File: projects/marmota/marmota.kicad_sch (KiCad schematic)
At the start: 58 parts, among them J1 USB_C, J2 Conn_01x20_Pin, J3 Conn_01x20_Pin, SW1 Button top, SW2 Button side, U1 RP2040, U2 FLASH, U3 MCP73871, U4 RT6150B, U5 ESP32, Y1 12MHz

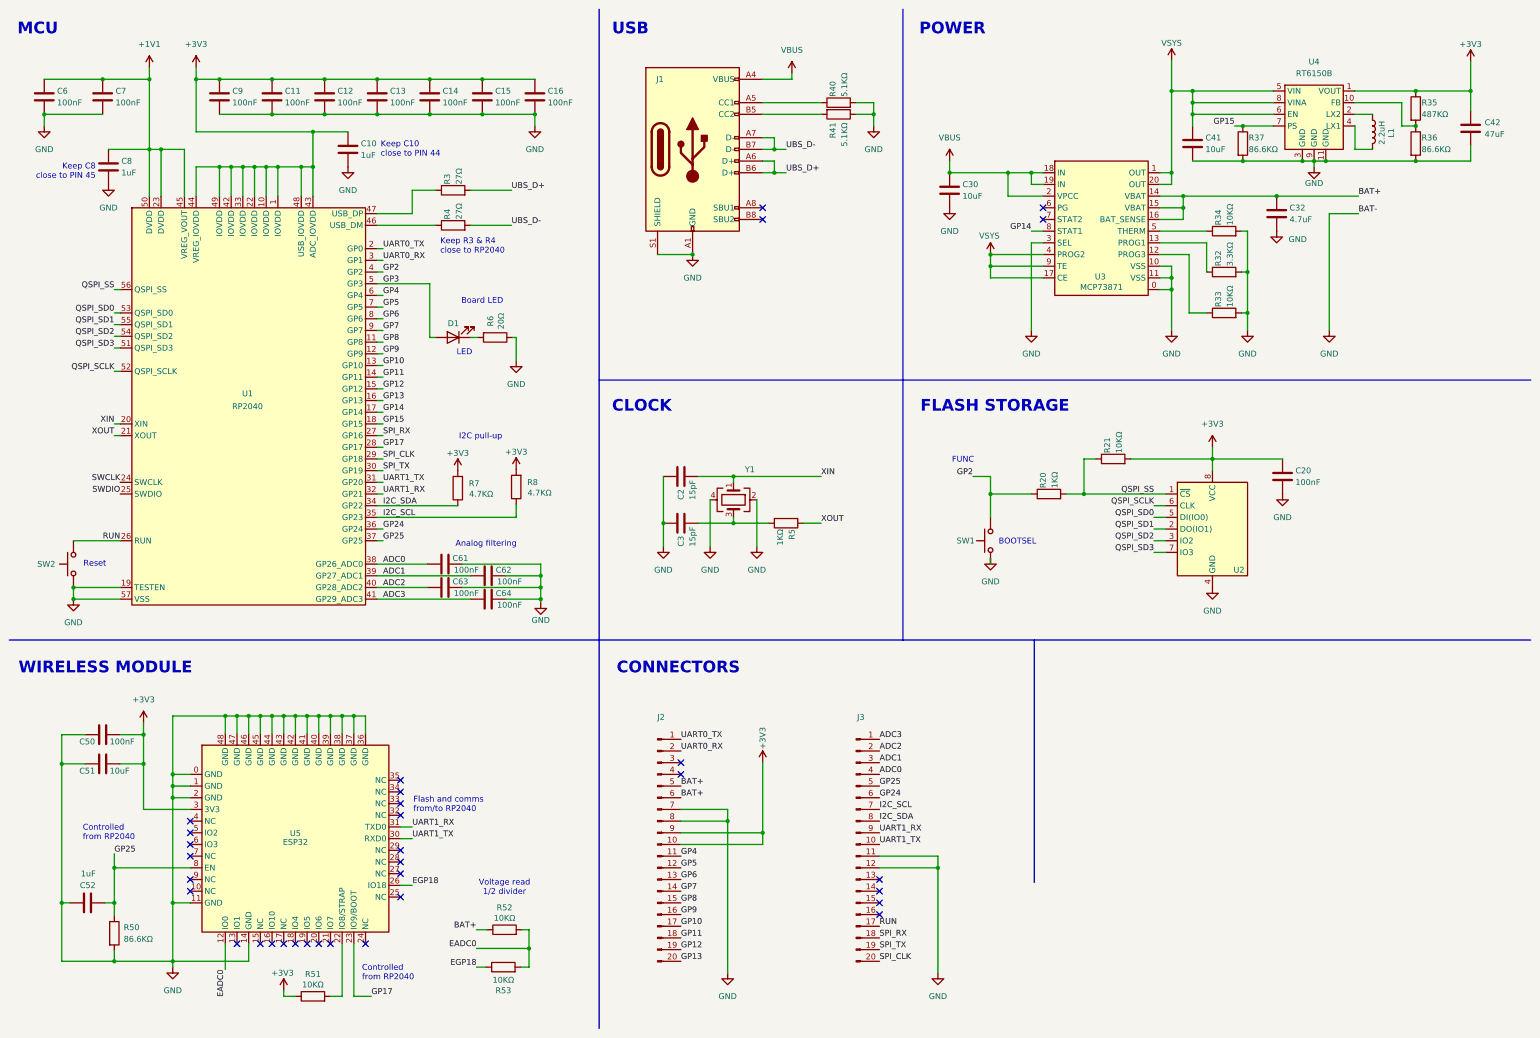
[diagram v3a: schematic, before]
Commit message: Initial schematic for nRF52840+nPM1300
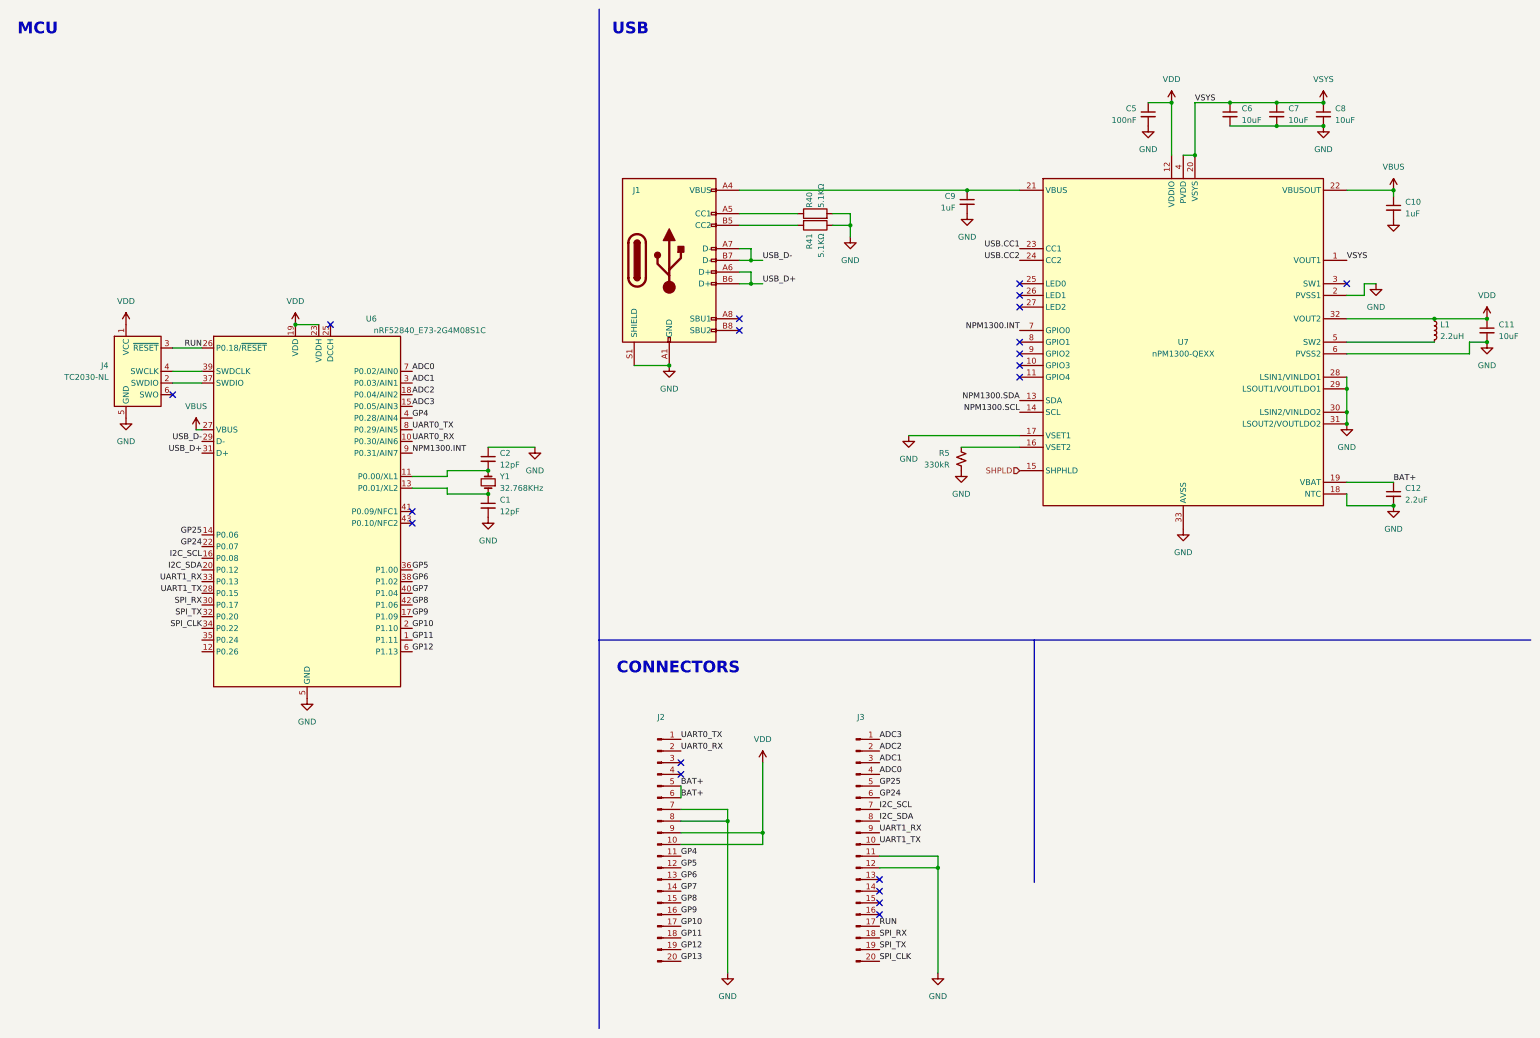
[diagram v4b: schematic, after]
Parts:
- removed C10, C52, C8: 1uF, ILO_fp:0402_compact, symbol Device:C
- removed C11, C12, C13, C14, C15, C16, C20, C50, C6, C61, C62, C63, C64, C7, C9: 100nF, ILO_fp:0402_compact, symbol Device:C
- removed C2, C3: 15pF, ILO_fp:0402_compact, symbol Device:C
- removed C30, C41, C51: 10uF, ILO_fp:0402_compact, symbol Device:C
- removed C32: 4.7uF, ILO_fp:0402_compact, symbol Device:C
- removed C42: 47uF, ILO_fp:0603_compact, symbol Device:C
- removed D1: Diode, ILO_fp:0603_d, symbol Device:LED
- removed L1: 2.2uH, ILO_fp:0603_compact, symbol Device:L
- removed R20, R5: 1KΩ, ILO_fp:0402_compact, symbol Device:R
- removed R21, R33, R34, R51, R52, R53: 10KΩ, ILO_fp:0402_compact, symbol Device:R
- removed R3, R4: 27Ω, ILO_fp:0402_compact, symbol Device:R
- removed R32: 3.3KΩ, ILO_fp:0402_compact, symbol Device:R
- removed R35: 487KΩ, ILO_fp:0402_compact, symbol Device:R
- removed R36, R37, R50: 86.6KΩ, ILO_fp:0402_compact, symbol Device:R
- removed R6: 20Ω, ILO_fp:0603, symbol Device:R
- removed R7, R8: 4.7KΩ, ILO_fp:0402_compact, symbol Device:R
- removed SW1: Button top, ILO_fp:Alpsalpine_SKRP_compact, symbol Switch:SW_Push
- removed SW2: Button side, ILO_fp:Alpsalpine_SKSC, symbol Switch:SW_Push
- removed U1: RP2040, Package_DFN_QFN:QFN-56-1EP_7x7mm_P0.4mm_EP3.2x3.2mm, symbol ILO_sym:Raspberry_RP2040
- removed U2: FLASH, ILO_fp:Winbond_W25Q, symbol Memory_Flash:W25Q128JVS
- removed U3: MCP73871, ILO_fp:QFN20_internal_routing, symbol ILO_sym:Microchip_MCP73871
- removed U4: RT6150B, ILO_fp:WDFN-10L-2.5x2.5, symbol ILO_sym:Richtek_RT6150
- removed U5: ESP32, ILO_fp:Espressif_ESP32_mini, symbol ILO_sym:Espressif_ESP8684_mini
- removed Y1: 12MHz, Crystal:Crystal_SMD_2520-4Pin_2.5x2.0mm, symbol Device:Crystal_GND24
- added C1, C2: 12pF, symbol Device:C_Small
- added C10, C9: 1uF, Capacitor_SMD:C_0603_1608Metric, symbol Device:C_Small
- added C11, C6, C7, C8: 10uF, Capacitor_SMD:C_0603_1608Metric, symbol Device:C_Small
- added C12: 2.2uF, Capacitor_SMD:C_0603_1608Metric, symbol Device:C_Small
- added C5: 100nF, Capacitor_SMD:C_0402_1005Metric, symbol Device:C_Small
- added J4: TC2030-NL, Connector:Tag-Connect_TC2030-IDC-NL_2x03_P1.27mm_Vertical, symbol Connector:Conn_ARM_SWD_TagConnect_TC2030-NL
- added L1: 2.2uH, Inductor_SMD:L_0603_1608Metric, symbol Device:L_Small
- added R5: 330kR, Resistor_SMD:R_0402_1005Metric, symbol Device:R_Small_US
- added U6: nRF52840_E73-2G4M08S1C, PCM_marbastlib-various:nRF52840_E73-2G4M08S1C, symbol PCM_marbastlib-various:nRF52840_E73-2G4M08S1C
- added U7: nPM1300-QEXX, Package_DFN_QFN:QFN-32-1EP_5x5mm_P0.5mm_EP3.6x3.6mm_ThermalVias, symbol nordic-lib-kicad-npm:nPM1300-QEXX
- added Y1: 32.768KHz, symbol Device:Crystal_Small
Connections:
- net ADC0: now also U6.7 (P0.02/AIN0)
- net ADC1: now also U6.3 (P0.03/AIN1)
- net ADC2: now also U6.18 (P0.04/AIN2)
- net ADC3: now also U6.15 (P0.05/AIN3)
- net BAT+: now also C12.1, U7.19 (VBAT)
- net GND: now also C1.2, C10.2, C11.2, C12.2, C2.1, C5.2, C6.2, C7.2, C8.2, C9.2, J4.5 (GND), R5.2, U6.21 (GND), U6.24 (GND), U6.5 (GND), U7.17 (VSET1), U7.18 (NTC), U7.2 (PVSS1), U7.28 (LSIN1/VINLDO1), U7.29 (LSOUT1/VOUTLDO1), U7.30 (LSIN2/VINLDO2), U7.31 (LSOUT2/VOUTLDO2), U7.33 (AVSS), U7.6 (PVSS2)
- net GP10: now also U6.2 (P1.10)
- net GP11: now also U6.1 (P1.11)
- net GP12: now also U6.6 (P1.13)
- net GP24: now also U6.22 (P0.07)
- net GP25: now also U6.14 (P0.06)
- net GP4: now also U6.4 (P0.28/AIN4)
- net GP5: now also U6.36 (P1.00)
- net GP6: now also U6.38 (P1.02)
- net GP7: now also U6.40 (P1.04)
- net GP8: now also U6.42 (P1.06)
- net GP9: now also U6.17 (P1.09)
- net I2C_SCL: now also U6.16 (P0.08)
- net I2C_SDA: now also U6.20 (P0.12)
- net RUN: now also J4.3 (~{RESET}), U6.26 (P0.18/~{RESET})
- net SPI_CLK: now also U6.34 (P0.22)
- net SPI_RX: now also U6.30 (P0.17)
- net SPI_TX: now also U6.32 (P0.20)
- net UART0_RX: now also U6.10 (P0.30/AIN6)
- net UART0_TX: now also U6.8 (P0.29/AIN5)
- net UART1_RX: now also U6.33 (P0.13)
- net UART1_TX: now also U6.28 (P0.15)
- net VBUS: now also C10.1, U6.27 (VBUS), U7.22 (VBUSOUT); no longer J1.A4 (VBUS), J1.A9 (VBUS), J1.B4 (VBUS), J1.B9 (VBUS)
- net VSYS: now also C6.1, C7.1, C8.1, U7.1 (VOUT1), U7.20 (VSYS), U7.4 (PVDD)
- net +3V3 renamed VDD
- net VDD: now also C11.1, C5.1, J4.1 (VCC), L1.1, U6.19 (VDD), U6.23 (VDDH), U7.12 (VDDIO), U7.32 (VOUT2)
- net UBS_D+ renamed USB_D+
- net USB_D+: now also U6.31 (D+)
- net UBS_D- renamed USB_D-
- net USB_D-: now also U6.29 (D-)
- new net: L1.2, U7.5 (SW2)
- new net: J4.2 (SWDIO), U6.37 (SWDIO)
- new net: J4.4 (SWCLK), U6.39 (SWDCLK)
- new net: C9.1, J1.A4 (VBUS), J1.A9 (VBUS), J1.B4 (VBUS), J1.B9 (VBUS), U7.21 (VBUS)
- new net: C1.1, U6.13 (P0.01/XL2), Y1.1
- new net: C2.2, U6.11 (P0.00/XL1), Y1.2
- new net: R5.1, U7.16 (VSET2)
- new net NPM1300.INT: U6.9 (P0.31/AIN7), U7.7 (GPIO0)
- new net NPM1300.SCL: U7.14 (SCL)
- new net NPM1300.SDA: U7.13 (SDA)
- new net SHPLD: U7.15 (SHPHLD)
- new net USB.CC1: U7.23 (CC1)
- new net USB.CC2: U7.24 (CC2)
- no-connect marks 33 -> 20
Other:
- note removed: "Analog filtering"
- note removed: "BOOTSEL"
- note removed: "Board LED"
- note removed: "CLOCK"
- note removed: "Controlled from RP2040"
- note removed: "FLASH STORAGE"
- note removed: "FUNC"
- note removed: "Flash and comms from/to RP2040"
- note removed: "I2C pull-up"
- note removed: "Keep C10 close to PIN 44"
- note removed: "Keep C8 close to PIN 45"
- note removed: "Keep R3 & R4 close to RP2040"
- note removed: "LED"
- note removed: "POWER"
- note removed: "Reset"
- note removed: "Voltage read 1/2 divider"
- note removed: "WIRELESS MODULE"
- moved on the sheet: J1, R40, R41

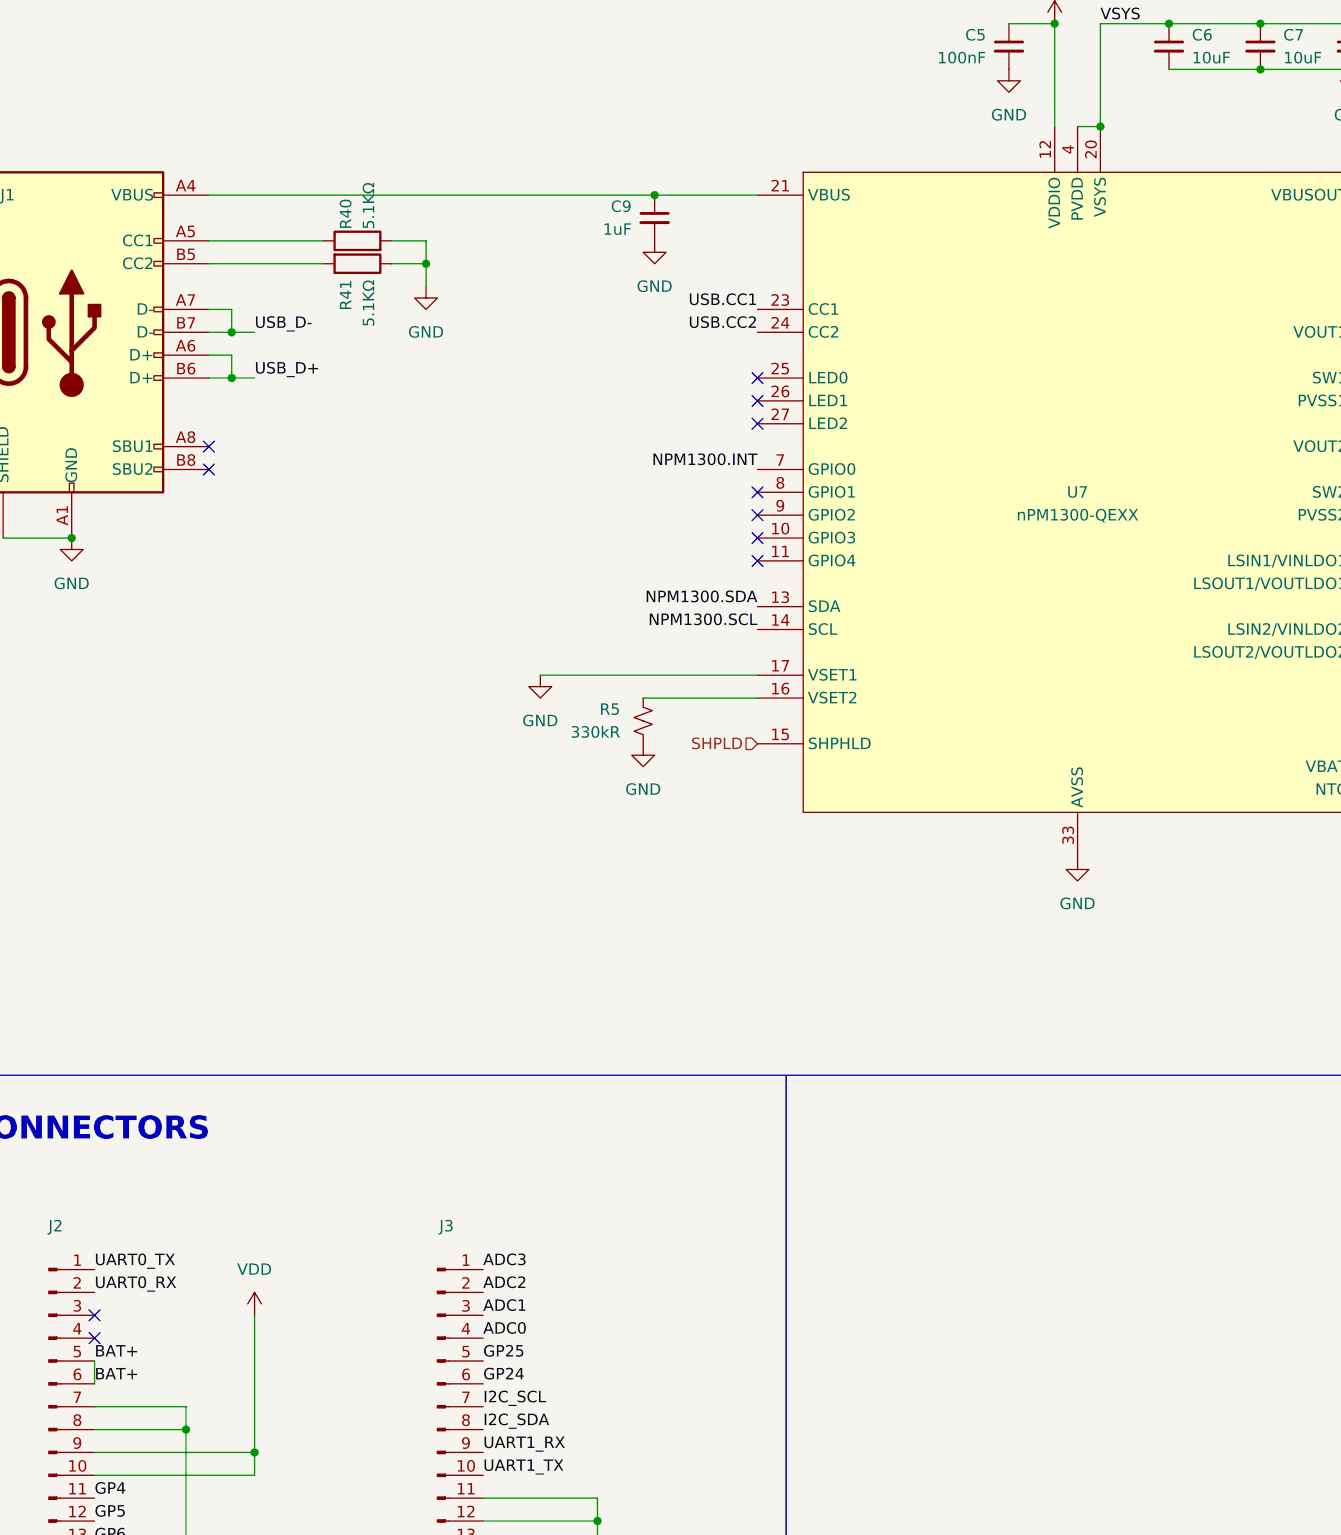
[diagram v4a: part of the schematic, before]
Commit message: Reworked Alpakka w/ interrupt lines, etc
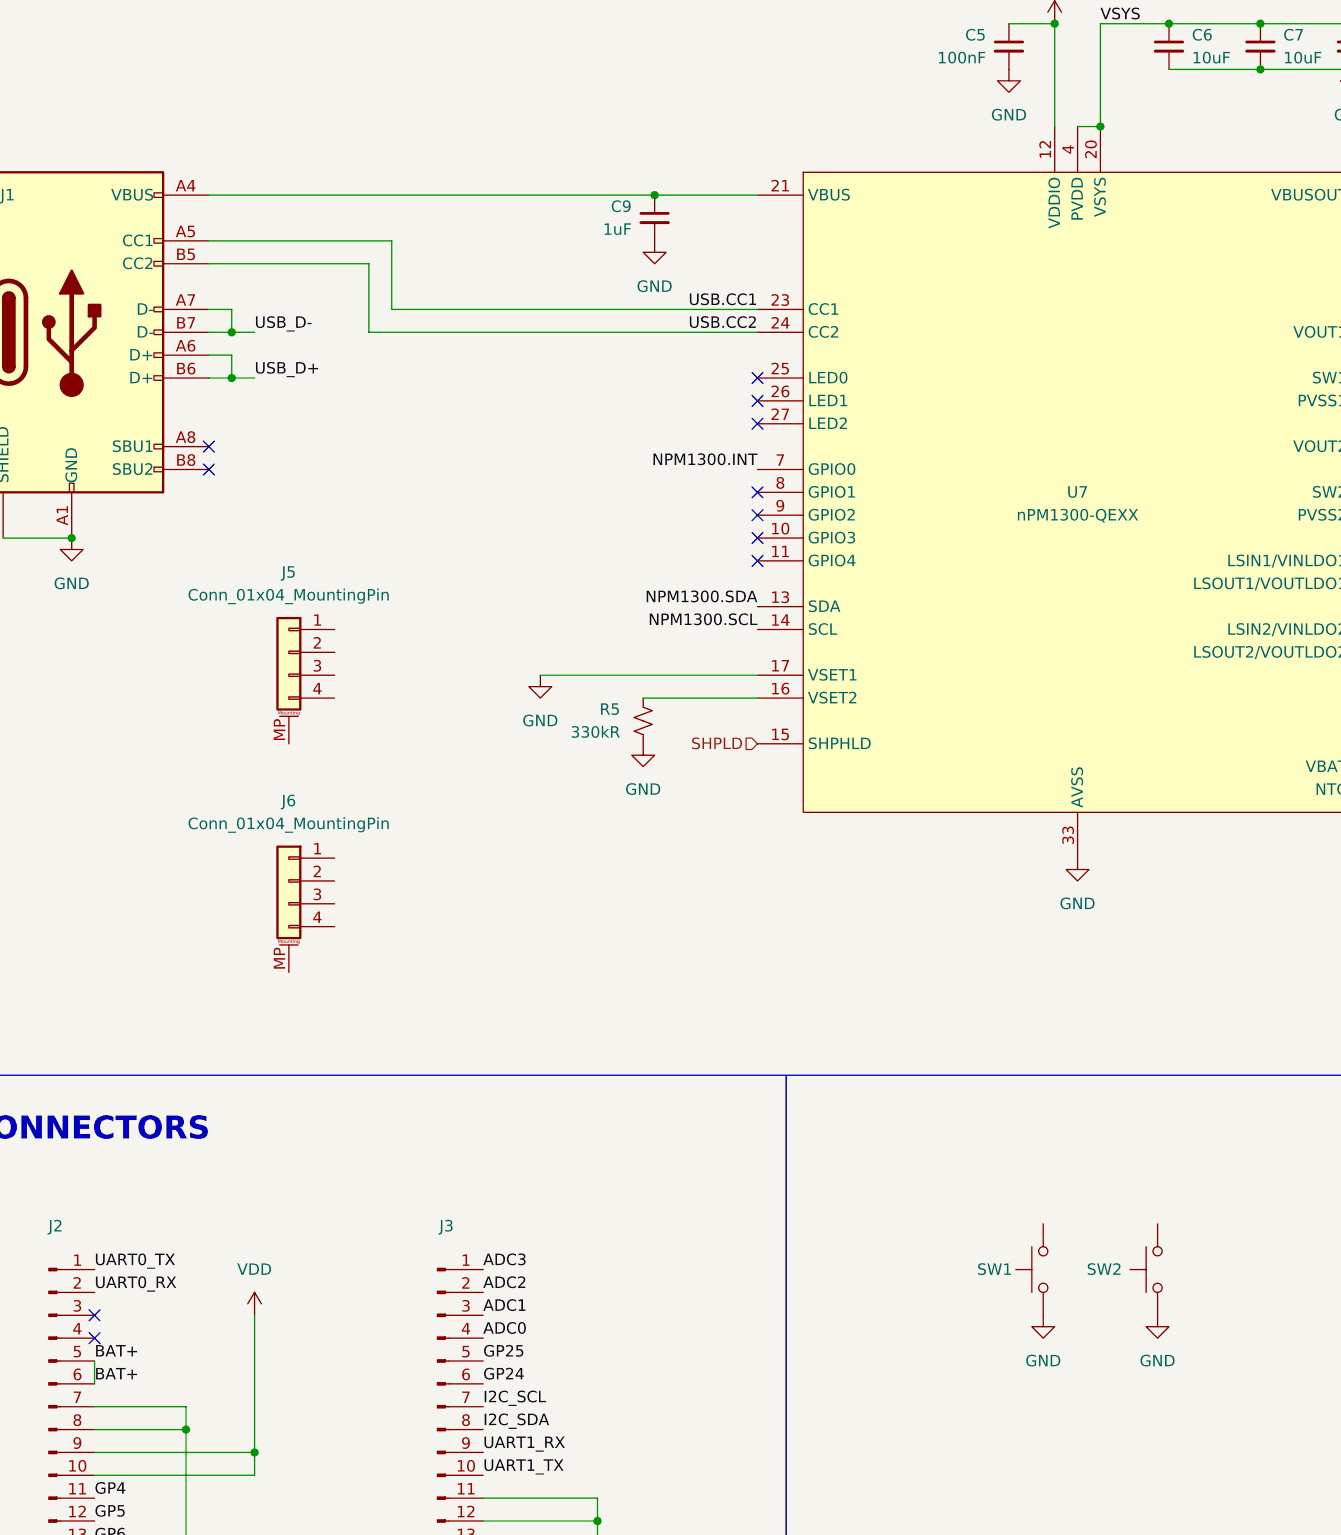
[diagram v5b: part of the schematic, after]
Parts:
- removed R40, R41: 5.1KΩ, ILO_fp:0402_compact, symbol Device:R
- added J5, J6: Conn_01x04_MountingPin, Connector_JST:JST_SH_SM04B-SRSS-TB_1x04-1MP_P1.00mm_Horizontal, symbol Connector_Generic_MountingPin:Conn_01x04_MountingPin
- added SW1: Button top, ILO_fp:Alpsalpine_SKRP_compact, symbol Switch:SW_Push
- added SW2: Button side, ILO_fp:Alpsalpine_SKSC, symbol Switch:SW_Push
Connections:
- net GND: now also SW1.1, SW2.1
- net USB.CC1: now also J1.A5 (CC1)
- net USB.CC2: now also J1.B5 (CC2)
